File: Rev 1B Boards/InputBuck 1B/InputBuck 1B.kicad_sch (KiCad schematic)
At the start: 3 parts, among them J16 Banana 2P, J17 Banana 2P, J23 Conn_01x01_Pin

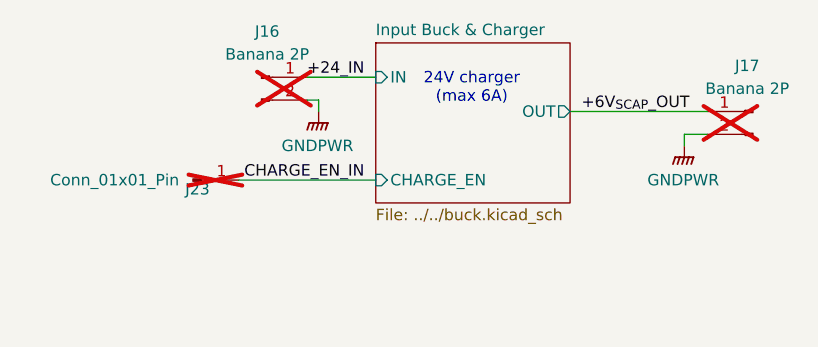
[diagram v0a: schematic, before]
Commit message: Polish input buck test board
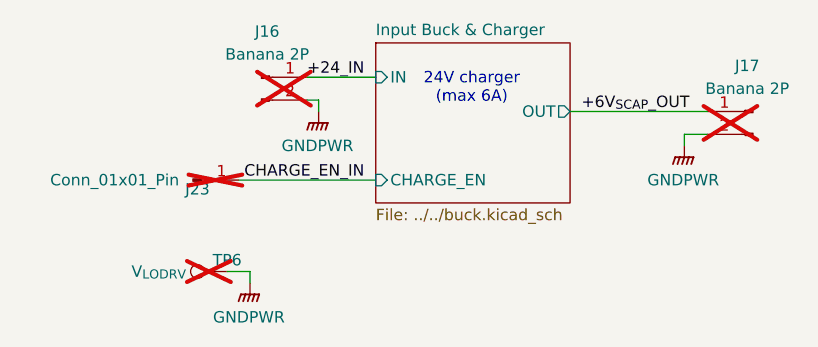
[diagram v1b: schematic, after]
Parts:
- added TP6: V_{LODRV}, TestPoint:TestPoint_Bridge_Pitch2.0mm_Drill0.7mm, symbol Connector:TestPoint
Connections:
- net GNDPWR: now also TP6.1
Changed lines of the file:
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@@
+	(wire
+		(pts
+			(xy 115.57 113.03) (xy 115.57 114.3)
+		)
+		(stroke
+			(width 0)
+			(type default)
+		)
+	)
+	(wire
+		(pts
+			(xy 113.03 113.03) (xy 115.57 113.03)
+		)
+		(stroke
+			(width 0)
+			(type default)
+		)
+	)
 	(wire
 		(pts
@@
 	)
 	(symbol
+		(lib_id "power:GNDPWR")
+		(at 115.57 114.3 0)
+		(unit 1)
+		(exclude_from_sim no)
+		(in_bom yes)
+		(on_board yes)
+		(dnp no)
+		(property "Reference" "#PWR020"
+			(at 115.57 119.38 0)
+			(effects
+				(font
+					(size 1.27 1.27)
+				)
+				(hide yes)
+			)
+		)
+		(property "Value" "GNDPWR"
+			(at 115.443 118.11 0)
+			(effects
+				(font
+					(size 1.27 1.27)
+				)
+			)
+		)
+		(property "Footprint" ""
+			(at 115.57 115.57 0)
+			(effects
+				(font
+					(size 1.27 1.27)
+				)
+				(hide yes)
+			)
+		)
+		(property "Datasheet" ""
+			(at 115.57 115.57 0)
+			(effects
+				(font
+					(size 1.27 1.27)
+				)
+				(hide yes)
+			)
+		)
+		(property "Description" "Power symbol creates a global label with name \"GNDPWR\" , global ground"
+			(at 115.57 114.3 0)
+			(effects
+				(font
+					(size 1.27 1.27)
+				)
+				(hide yes)
+			)
+		)
+		(pin "1"
+		)
+		(instances
+			(project "InputBuck 1B"
+				(path "/cd2154d9-e30e-4705-b0ff-30d832f32d72"
+					(reference "#PWR020")
+					(unit 1)
+				)
+			)
+		)
+	)
+	(symbol
 		(lib_id "Connector:Conn_01x02_Pin")
 		(at 116.84 91.44 0)
@@
 					(unit 1)
 				)
+			)
+		)
+	)
+	(symbol
+		(lib_id "Connector:TestPoint")
+		(at 113.03 113.03 90)
+		(unit 1)
+		(exclude_from_sim no)
+		(in_bom yes)
+		(on_board yes)
+		(dnp yes)
+		(property "Reference" "TP6"
+			(at 113.03 111.76 90)
+			(effects
+				(font
+					(size 1.27 1.27)
+				)
+			)
+		)
+		(property "Value" "V_{LODRV}"
+			(at 108.458 113.03 90)
+			(effects
+				(font
+					(size 1.27 1.27)
+				)
+				(justify left)
+			)
+		)
+		(property "Footprint" "TestPoint:TestPoint_Bridge_Pitch2.0mm_Drill0.7mm"
+			(at 113.03 107.95 0)
+			(effects
+				(font
+					(size 1.27 1.27)
+				)
+				(hide yes)
+			)
+		)
+		(property "Datasheet" "~"
+			(at 113.03 107.95 0)
+			(effects
+				(font
+					(size 1.27 1.27)
+				)
+				(hide yes)
+			)
+		)
+		(property "Description" "test point"
+			(at 113.03 113.03 0)
+			(effects
+				(font
+					(size 1.27 1.27)
+				)
+				(hide yes)
+			)
+		)
+		(property "Sim.Device" ""
+			(at 113.03 113.03 0)
+			(effects
+				(font
+					(size 1.27 1.27)
+				)
+			)
+		)
+		(property "Sim.Pins" ""
+			(at 113.03 113.03 0)
+			(effects
+				(font
+					(size 1.27 1.27)
+				)
+			)
+		)
+		(property "Sim.Type" ""
+			(at 113.03 113.03 0)
+			(effects
+				(font
+					(size 1.27 1.27)
+				)
+			)
+		)
+		(property "Height" ""
+			(at 113.03 113.03 0)
+			(effects
+				(font
+					(size 1.27 1.27)
+				)
+			)
+		)
+		(property "Manufacturer_Name" ""
+			(at 113.03 113.03 0)
+			(effects
+				(font
+					(size 1.27 1.27)
+				)
+			)
+		)
+		(property "Manufacturer_Part_Number" ""
+			(at 113.03 113.03 0)
+			(effects
+				(font
+					(size 1.27 1.27)
+				)
+			)
+		)
+		(property "Mouser Price/Stock" ""
+			(at 113.03 113.03 0)
+			(effects
+				(font
+					(size 1.27 1.27)
+				)
+			)
+		)
+		(pin "1"
+		)
+		(instances
+			(project "InputBuck 1B"
+				(path "/cd2154d9-e30e-4705-b0ff-30d832f32d72"
+					(reference "TP6")
+					(unit 1)
+				)

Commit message: Replace most banana jacks with XT connectors
+ update library
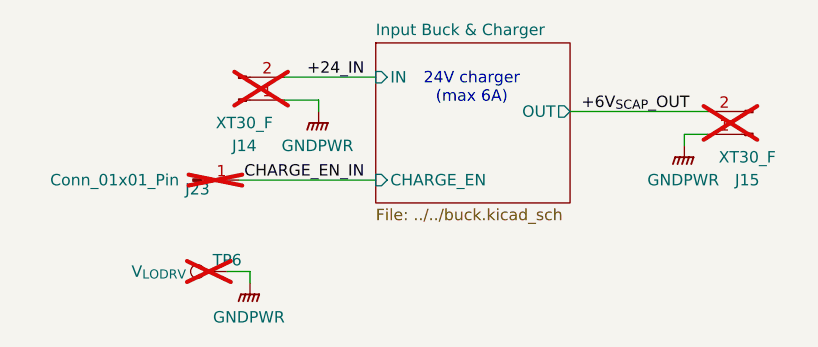
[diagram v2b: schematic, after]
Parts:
- removed J16, J17: Banana 2P, Connector:Banana_Jack_2Pin, symbol Connector:Conn_01x02_Pin
- added J14, J15: XT30_F, Connector_AMASS:AMASS_XT30U-F_1x02_P5.0mm_Vertical, symbol Connector:Conn_01x02_Pin
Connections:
- net +24_IN: now also J14.2 (Pin_2)
- net +6V_{SCAP}_OUT: now also J15.2 (Pin_2)
- net GNDPWR: now also J14.1 (Pin_1), J15.1 (Pin_1)
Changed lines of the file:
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@@
 	(wire
 		(pts
-			(xy 121.92 93.98) (xy 123.19 93.98)
+			(xy 119.38 93.98) (xy 123.19 93.98)
 		)
 		(stroke
@@
 	(wire
 		(pts
-			(xy 121.92 91.44) (xy 129.54 91.44)
+			(xy 119.38 91.44) (xy 129.54 91.44)
 		)
 		(stroke
@@
 	(symbol
 		(lib_id "Connector:Conn_01x02_Pin")
-		(at 171.45 95.25 0)
-		(mirror y)
+		(at 114.3 93.98 0)
+		(mirror x)
 		(unit 1)
 		(exclude_from_sim no)
@@
 		(on_board yes)
 		(dnp yes)
-		(property "Reference" "J17"
-			(at 170.815 90.17 0)
-			(effects
-				(font
-					(size 1.27 1.27)
-				)
-			)
-		)
-		(property "Value" "Banana 2P"
-			(at 170.815 92.71 0)
-			(effects
-				(font
-					(size 1.27 1.27)
-				)
-			)
-		)
-		(property "Footprint" "Connector:Banana_Jack_2Pin"
-			(at 171.45 95.25 0)
+		(property "Reference" "J14"
+			(at 114.935 99.06 0)
+			(effects
+				(font
+					(size 1.27 1.27)
+				)
+			)
+		)
+		(property "Value" "XT30_F"
+			(at 114.935 96.52 0)
+			(effects
+				(font
+					(size 1.27 1.27)
+				)
+			)
+		)
+		(property "Footprint" "Connector_AMASS:AMASS_XT30U-F_1x02_P5.0mm_Vertical"
+			(at 114.3 93.98 0)
 			(effects
 				(font
@@
 		)
 		(property "Datasheet" "~"
-			(at 171.45 95.25 0)
+			(at 114.3 93.98 0)
 			(effects
 				(font
@@
 		)
 		(property "Description" "Generic connector, single row, 01x02, script generated"
-			(at 171.45 95.25 0)
+			(at 114.3 93.98 0)
 			(effects
 				(font
@@
 		)
 		(property "Sim.Device" ""
-			(at 171.45 95.25 0)
+			(at 114.3 93.98 0)
 			(effects
 				(font
@@
 		)
 		(property "Sim.Pins" ""
-			(at 171.45 95.25 0)
+			(at 114.3 93.98 0)
 			(effects
 				(font
@@
 		)
 		(property "Sim.Type" ""
-			(at 171.45 95.25 0)
+			(at 114.3 93.98 0)
 			(effects
 				(font
@@
 		)
 		(property "Height" ""
-			(at 171.45 95.25 0)
+			(at 114.3 93.98 0)
 			(effects
 				(font
@@
 		)
 		(property "Manufacturer_Name" ""
-			(at 171.45 95.25 0)
+			(at 114.3 93.98 0)
 			(effects
 				(font
@@
 		)
 		(property "Manufacturer_Part_Number" ""
-			(at 171.45 95.25 0)
+			(at 114.3 93.98 0)
 			(effects
 				(font
@@
 		)
 		(property "Mouser Price/Stock" ""
-			(at 171.45 95.25 0)
+			(at 114.3 93.98 0)
 			(effects
 				(font
@@
 			(project "InputBuck 1B"
 				(path "/cd2154d9-e30e-4705-b0ff-30d832f32d72"
-					(reference "J17")
+					(reference "J14")
 					(unit 1)
 				)
@@
 	(symbol
 		(lib_id "Connector:Conn_01x02_Pin")
-		(at 116.84 91.44 0)
+		(at 171.45 97.79 180)
 		(unit 1)
 		(exclude_from_sim no)
@@
 		(on_board yes)
 		(dnp yes)
-		(property "Reference" "J16"
-			(at 117.475 86.36 0)
-			(effects
-				(font
-					(size 1.27 1.27)
-				)
-			)
-		)
-		(property "Value" "Banana 2P"
-			(at 117.475 88.9 0)
-			(effects
-				(font
-					(size 1.27 1.27)
-				)
-			)
-		)
-		(property "Footprint" "Connector:Banana_Jack_2Pin"
-			(at 116.84 91.44 0)
+		(property "Reference" "J15"
+			(at 170.815 102.87 0)
+			(effects
+				(font
+					(size 1.27 1.27)
+				)
+			)
+		)
+		(property "Value" "XT30_F"
+			(at 170.815 100.33 0)
+			(effects
+				(font
+					(size 1.27 1.27)
+				)
+			)
+		)
+		(property "Footprint" "Connector_AMASS:AMASS_XT30U-F_1x02_P5.0mm_Vertical"
+			(at 171.45 97.79 0)
 			(effects
 				(font
@@
 		)
 		(property "Datasheet" "~"
-			(at 116.84 91.44 0)
+			(at 171.45 97.79 0)
 			(effects
 				(font
@@
 		)
 		(property "Description" "Generic connector, single row, 01x02, script generated"
-			(at 116.84 91.44 0)
+			(at 171.45 97.79 0)
 			(effects
 				(font
@@
 		)
 		(property "Sim.Device" ""
-			(at 116.84 91.44 0)
+			(at 171.45 97.79 0)
 			(effects
 				(font
@@
 		)
 		(property "Sim.Pins" ""
-			(at 116.84 91.44 0)
+			(at 171.45 97.79 0)
 			(effects
 				(font
@@
 		)
 		(property "Sim.Type" ""
-			(at 116.84 91.44 0)
+			(at 171.45 97.79 0)
 			(effects
 				(font
@@
 		)
 		(property "Height" ""
-			(at 116.84 91.44 0)
+			(at 171.45 97.79 0)
 			(effects
 				(font
@@
 		)
 		(property "Manufacturer_Name" ""
-			(at 116.84 91.44 0)
+			(at 171.45 97.79 0)
 			(effects
 				(font
@@
 		)
 		(property "Manufacturer_Part_Number" ""
-			(at 116.84 91.44 0)
+			(at 171.45 97.79 0)
 			(effects
 				(font
@@
 		)
 		(property "Mouser Price/Stock" ""
-			(at 116.84 91.44 0)
+			(at 171.45 97.79 0)
 			(effects
 				(font
@@
 			(project "InputBuck 1B"
 				(path "/cd2154d9-e30e-4705-b0ff-30d832f32d72"
-					(reference "J16")
+					(reference "J15")
 					(unit 1)
 				)
